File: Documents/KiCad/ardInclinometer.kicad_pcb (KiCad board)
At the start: 2 copper layers, 45.1 x 81.3 mm, 19 parts, among them J1 2-pin_power_input_header, J2 4-pin_I2C_LCD_header, U1 6-pin_5_button_header, U2 6-pin_5_LED_header, U3 MPU-6050

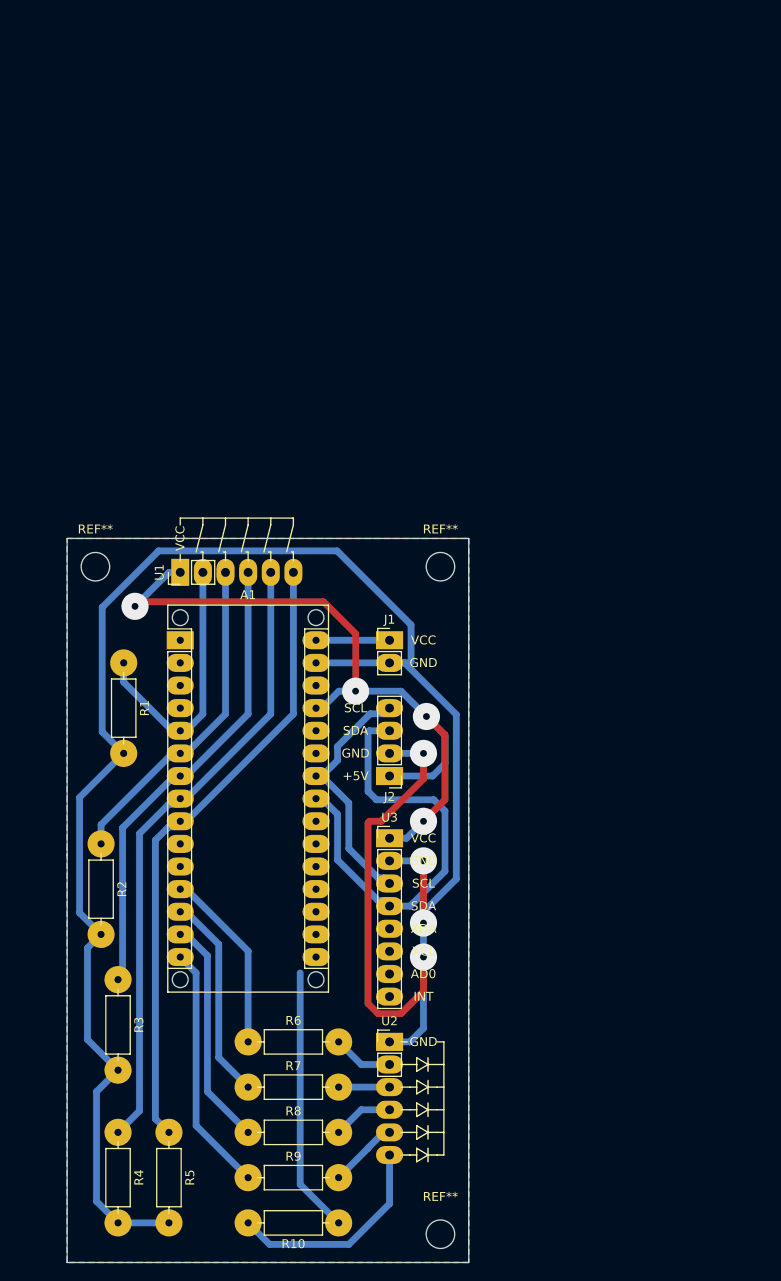
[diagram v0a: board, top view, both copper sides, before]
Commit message: uno casing and schematics
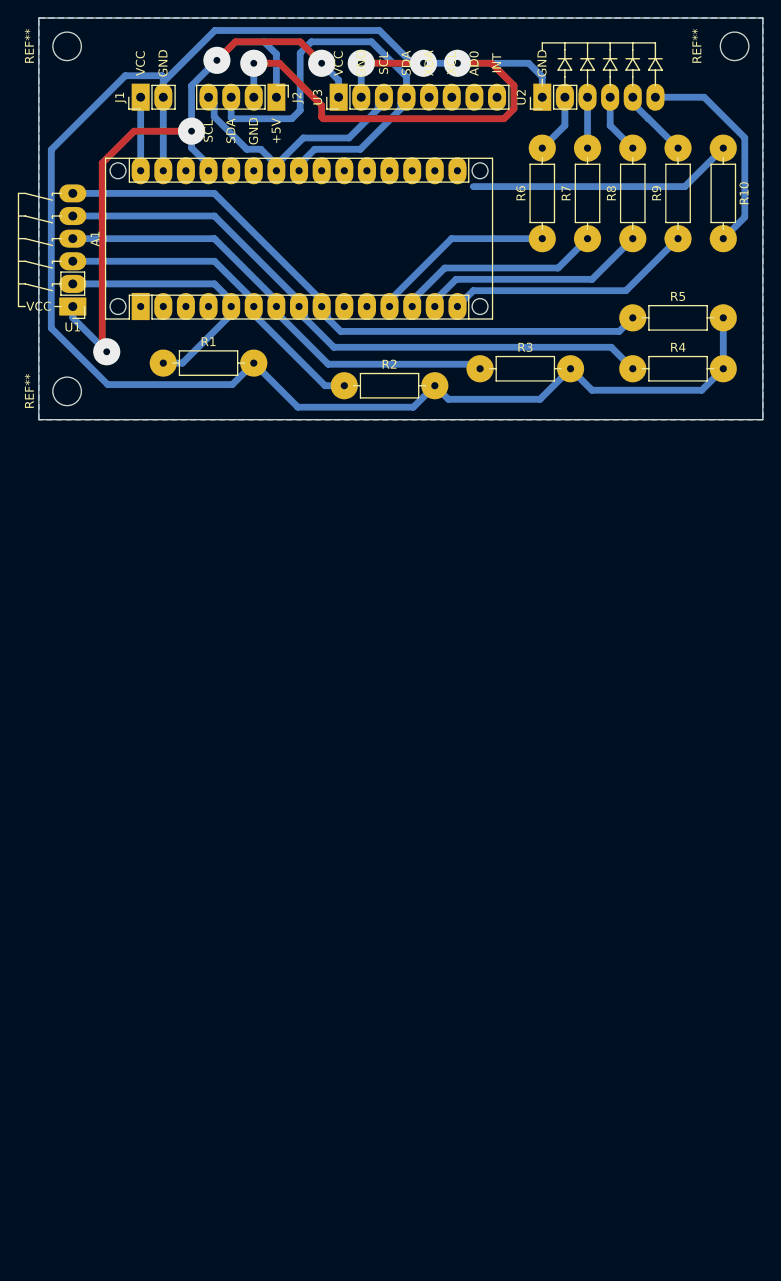
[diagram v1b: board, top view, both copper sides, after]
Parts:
- moved REF** 137.4 mm to (192.4, -1.91), turned to 90 degrees
- moved R10 128.1 mm to (191.1, 9.53), turned to 270 degrees
- moved R9 115.9 mm to (186.1, 19.7), turned to 90 degrees
- moved R8 109.2 mm to (181.0, 19.7), turned to 90 degrees
- moved U2 107.4 mm to (170.8, 3.81), turned to 90 degrees
- moved R5 105.2 mm to (181.0, 28.6), turned to 0 degrees
- moved R4 103.4 mm to (181.0, 34.3), turned to 0 degrees
- moved R7 102.6 mm to (175.9, 19.7), turned to 90 degrees
- moved R6 96.0 mm to (170.8, 19.7), turned to 90 degrees
- moved U3 83.4 mm to (148.0, 3.81), turned to 90 degrees
- moved R3 79.7 mm to (163.8, 34.3), turned to 0 degrees
- moved J2 77.3 mm to (141.0, 3.81), turned to 270 degrees
- moved REF** 71.9 mm to (117.5, -1.91), turned to 90 degrees
- moved J1 67.1 mm to (125.7, 3.81), turned to 90 degrees
- moved R2 58.2 mm to (148.6, 36.2), turned to 0 degrees
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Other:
- board size 45.1 x 81.3 mm -> 81.3 x 45.1 mm
